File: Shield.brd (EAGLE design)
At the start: 99.1 x 71.1 mm, 77 parts

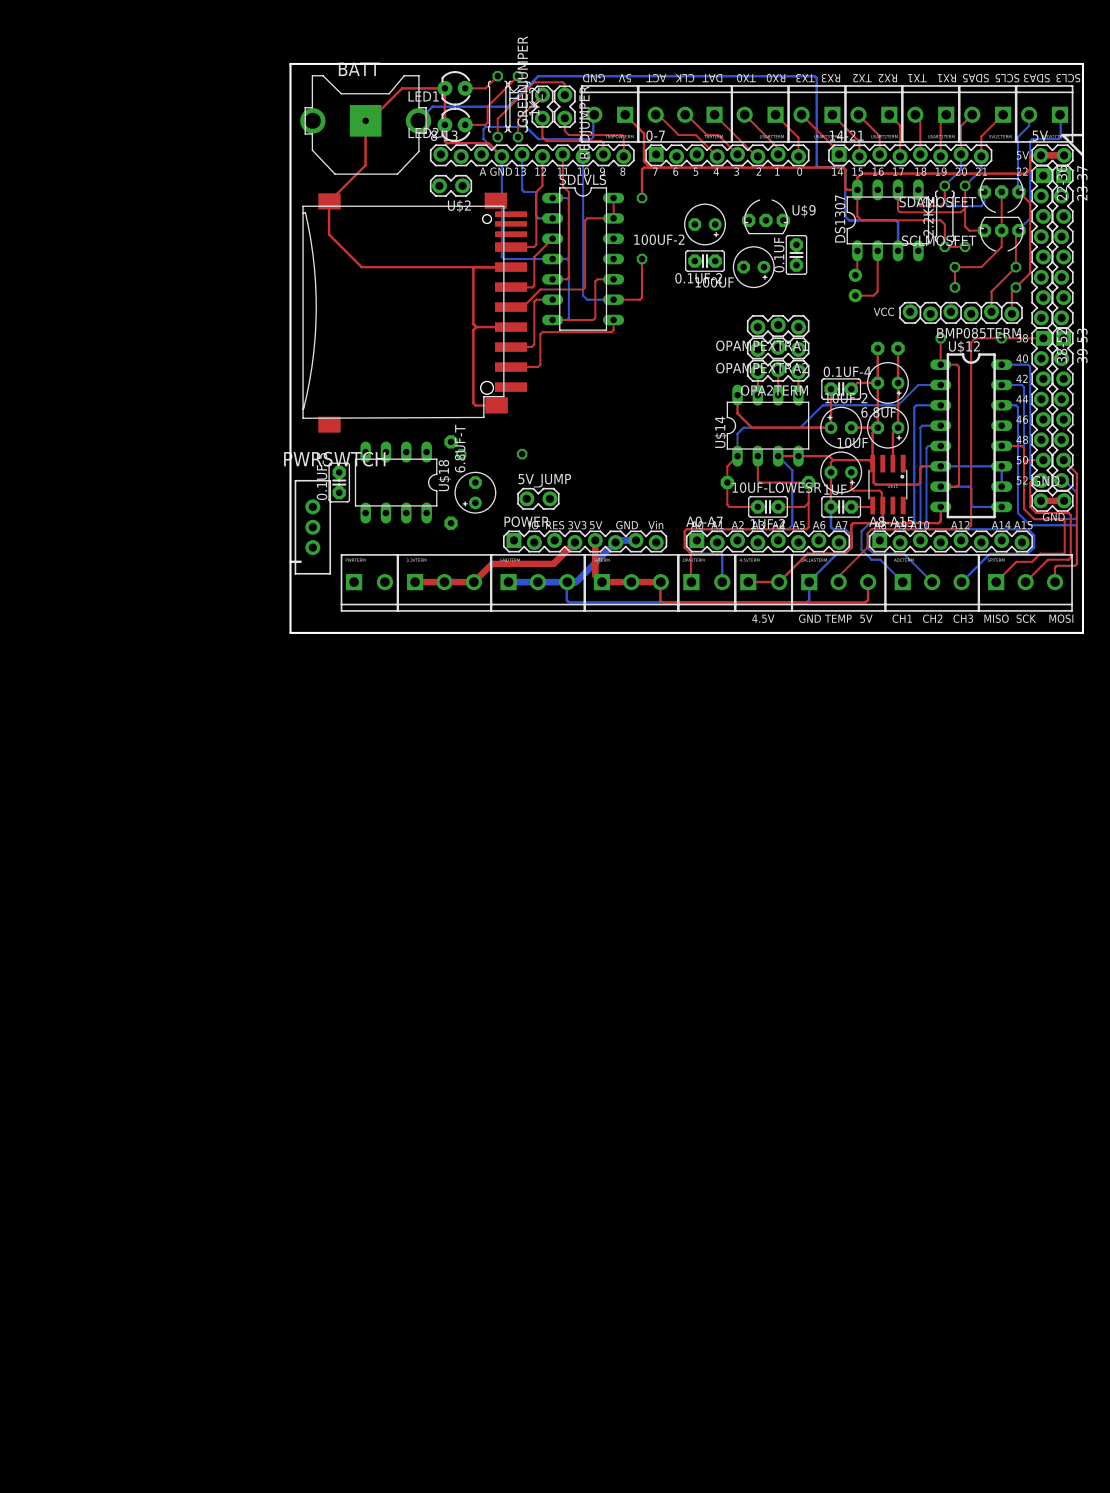
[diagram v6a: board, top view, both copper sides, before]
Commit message: Added charging circuit to schematic
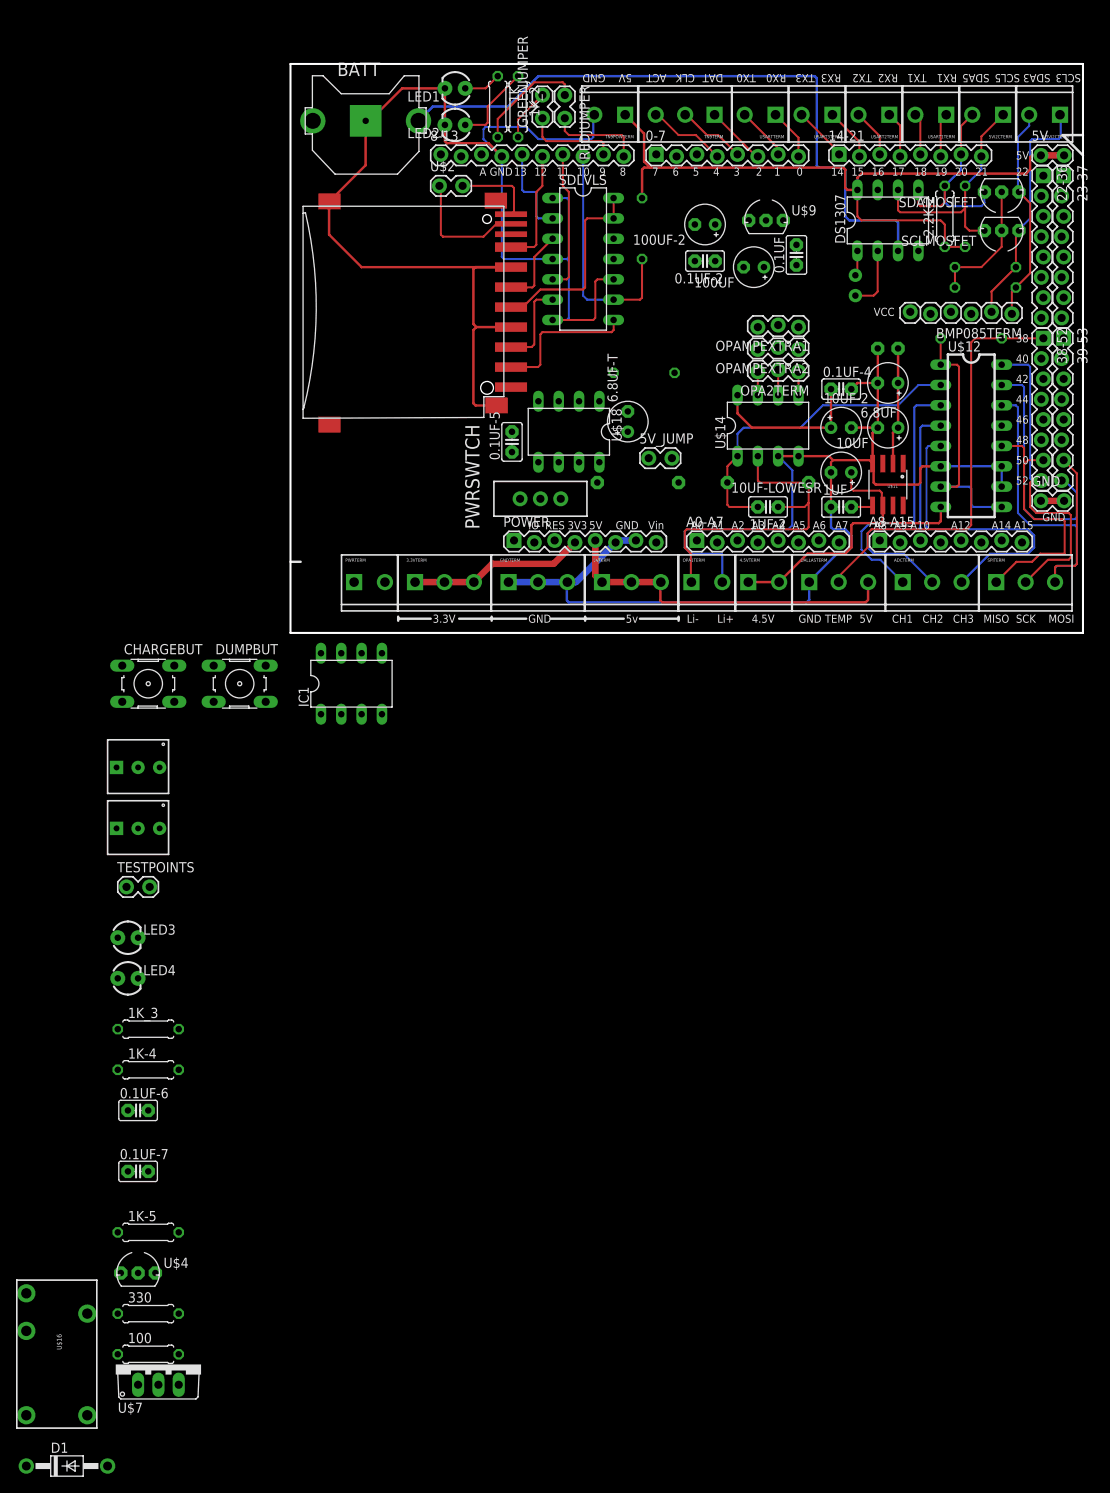
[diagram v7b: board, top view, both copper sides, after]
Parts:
- added 0.1UF-6, 0.1UF-7: CCL, LEMS:C025-025X050
- added 100, 1K-4, 1K-5, 1K_3, 330: RT, LEMS:0207/7
- added CHARGEBUT, DUMPBUT: (no value), LEMS:B3F-10XX
- added D1: 1N4004, LEMS:DO41-10
- added IC1: NE555P, LEMS:DIL-08
- added LED3, LED4: (no value), LEMS:LED3MM
- added TESTPOINTS: 2PHN, LEMS:2PH
- added TRESPOT, TRIGPOT: TRIMPOTT, LEMS:TRIMPOT_PTH_S3_LOCK
- added U$16: RELAYPTH4, LEMS:RELAY-JZC
- added U$4: 2N2222T, LEMS:TO-92INLINE
- added U$7: IRLZ34T, LEMS:TO220V
- moved PWRSWTCH 28.7 mm to (31.2, 16.8), turned to 90 degrees
- moved 250K 23.4 mm to (43.4, 18.8), turned to 180 degrees
- moved U$18 22.5 mm to (34.8, 25.1)
- moved 0.1UF-5 22.2 mm to (27.7, 23.9)
- moved 1 21.6 mm to (44.2, 32.5)
- moved 6.8UF-T 21.0 mm to (42.2, 26.4)
- moved 5V_JUMP 16.1 mm to (46.2, 21.8)
- turned U$2 to 0 degrees
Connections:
- new net 555OUT: 1K-4.2, 1K-5.1, IC1.3
- new net DIS: IC1.7, LED3.K
- new net DUMMY: U$16.2
- new net N$10: 1K-4.1, LED4.A
- new net N$11: 100.1, 330.1, U$4.1
- new net N$12: 1K-5.2, U$4.2
- new net N$13: 100.2, U$7.1
- new net N$15: D1.A, U$16.1, U$7.2
- new net N$8: 1K_3.1, LED3.A
- new net N$9: 0.1UF-7.1, IC1.5
- new net SLRIN: U$16.4
- new net TP1: CHARGEBUT.3, CHARGEBUT.4, IC1.2, TESTPOINTS.1, TRIGPOT.2
- new net TP2: DUMPBUT.3, DUMPBUT.4, IC1.6, TESTPOINTS.2, TRESPOT.2
- net 5V: now also 0.1UF-6.2, 1K_3.2, 330.2, DUMPBUT.1, DUMPBUT.2, IC1.4, IC1.8
- net GND: now also 0.1UF-6.1, 0.1UF-7.2, CHARGEBUT.1, CHARGEBUT.2, IC1.1, LED4.K, TRESPOT.3, TRIGPOT.3, U$4.3, U$7.3
- net PWRN: now also D1.C, TRESPOT.1, TRIGPOT.1, U$16.3, U$16.5
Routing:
- net SD_CD: track 0.00 -> 15.7 mm
- net SD_WP: track 0.00 -> 9.98 mm
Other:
- board text added: "3.3V"
- board text added: "5v"
- board text added: "Li+"
- board text added: "Li-"

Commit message: Changed charging circuit, finished routing
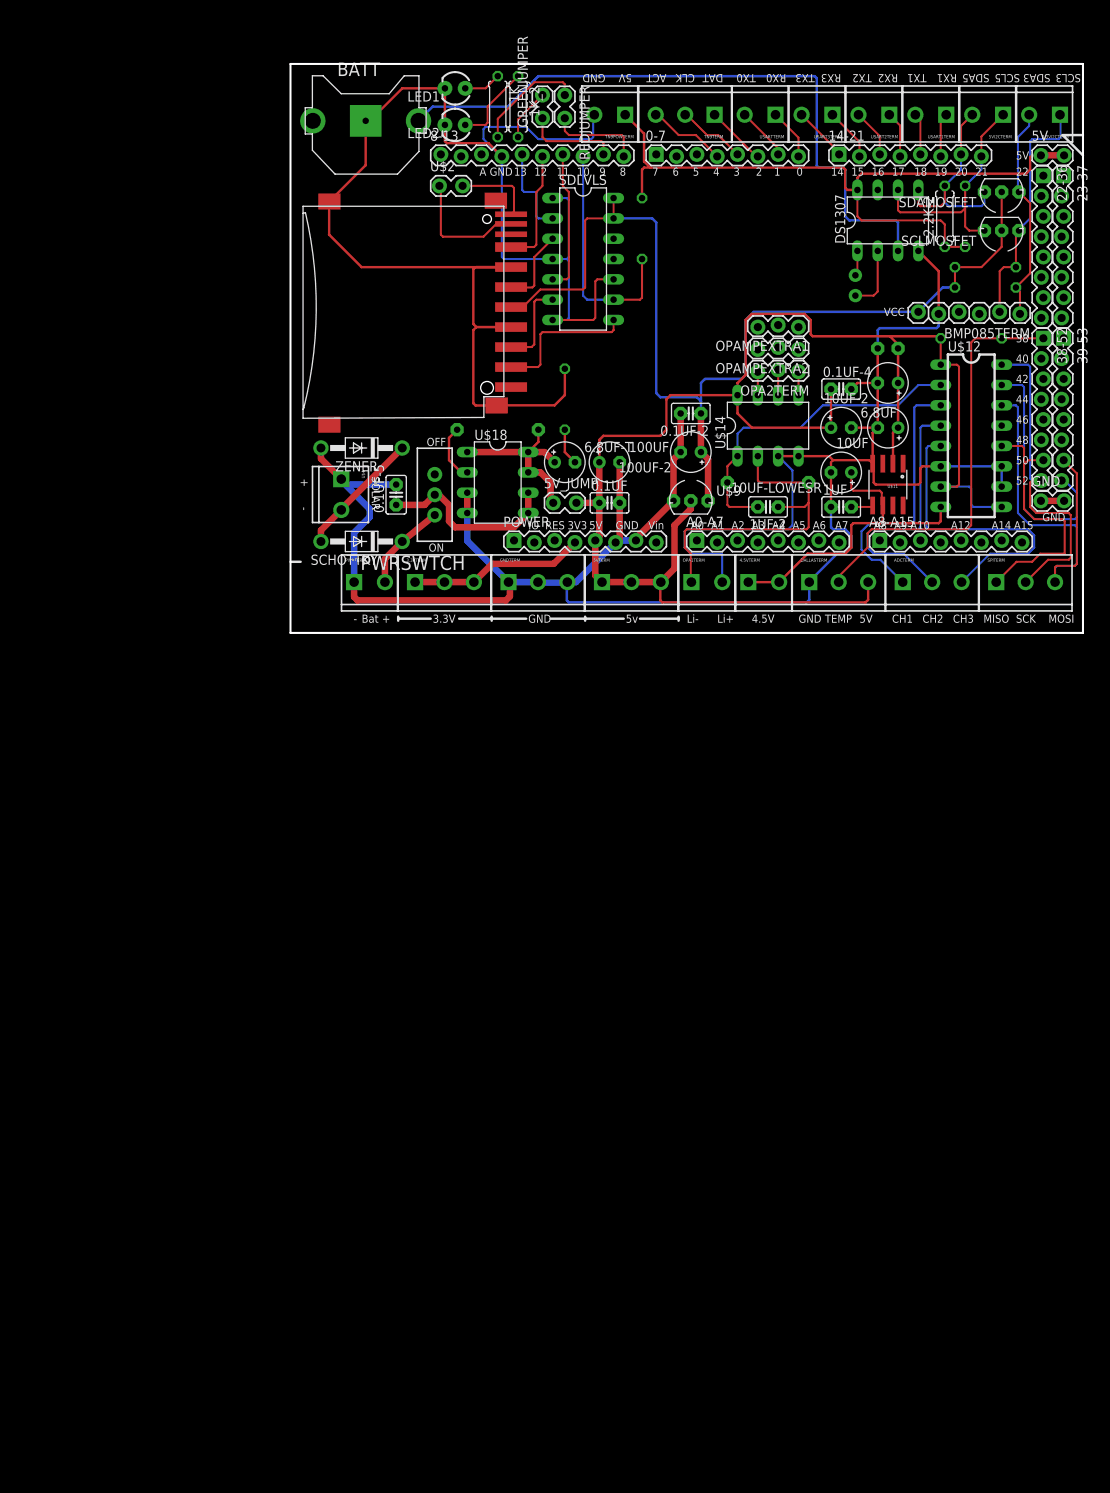
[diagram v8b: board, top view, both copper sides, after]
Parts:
- removed 0.1UF-6, 0.1UF-7: CCL, LEMS:C025-025X050
- removed 100, 1K-4, 1K-5, 1K_3, 330: RT, LEMS:0207/7
- removed CHARGEBUT, DUMPBUT: (no value), LEMS:B3F-10XX
- removed D1: 1N4004, LEMS:DO41-10
- removed IC1: NE555P, LEMS:DIL-08
- removed LED3, LED4: (no value), LEMS:LED3MM
- removed TESTPOINTS: 2PHN, LEMS:2PH
- removed TRESPOT, TRIGPOT: TRIMPOTT, LEMS:TRIMPOT_PTH_S3_LOCK
- removed U$16: RELAYPTH4, LEMS:RELAY-JZC
- removed U$7: IRLZ34T, LEMS:TO220V
- added SCHOTTKY: (no value), adafruit:DO41-10
- added ZENER: 1N4004, LEMS:DO41-10
- U$4: value 2N2222T -> 2PHS; device LEMS:TO-92INLINE -> LEMS:SCREWTERMINAL-3.5MM-2_LOCK
- moved U$4 102.3 mm to (6.35, 19.1), turned to 270 degrees
- moved 0.1UF 38.8 mm to (39.9, 16.3), turned to 0 degrees
- moved U$9 36.3 mm to (50.0, 16.5)
- moved 100UF 30.3 mm to (39.9, 21.3), turned to 0 degrees
- moved 100UF-2 28.5 mm to (50.0, 22.6)
- moved 0.1UF-2 19.1 mm to (50.0, 27.4)
- moved 250K 18.7 mm to (25.9, 25.4)
- moved 0.1UF-5 15.9 mm to (13.2, 17.3)
- moved PWRSWTCH 13.2 mm to (18.0, 17.3), turned to 180 degrees
- moved 5V_JUMP 13.2 mm to (34.3, 16.3)
- moved U$18 10.9 mm to (25.9, 18.8), turned to 270 degrees
- moved 1 10.4 mm to (34.3, 29.2), turned to 270 degrees
- moved 6.8UF-T 9.37 mm to (34.3, 21.3), turned to 0 degrees
- moved BMP085TERM 1.02 mm to (84.8, 39.9)
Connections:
- removed net 555OUT: 1K-4.2, 1K-5.1, IC1.3
- removed net DIS: IC1.7, LED3.K
- removed net DUMMY: U$16.2
- removed net N$10: 1K-4.1, LED4.A
- removed net N$11: 100.1, 330.1, U$4.1
- removed net N$12: 1K-5.2, U$4.2
- removed net N$13: 100.2, U$7.1
- removed net N$15: D1.A, U$16.1, U$7.2
- removed net N$8: 1K_3.1, LED3.A
- removed net N$9: 0.1UF-7.1, IC1.5
- removed net SLRIN: U$16.4
- removed net TP1: CHARGEBUT.3, CHARGEBUT.4, IC1.2, TESTPOINTS.1, TRIGPOT.2
- removed net TP2: DUMPBUT.3, DUMPBUT.4, IC1.6, TESTPOINTS.2, TRESPOT.2
- new net SOLRPOS: SCHOTTKY.A, U$4.2, ZENER.C
- net 5V: no longer 0.1UF-6.2, 1K_3.2, 330.2, DUMPBUT.1, DUMPBUT.2, IC1.4, IC1.8
- net GND: now also U$4.1, ZENER.A; no longer 0.1UF-6.1, 0.1UF-7.2, CHARGEBUT.1, CHARGEBUT.2, IC1.1, LED4.K, TRESPOT.3, TRIGPOT.3, U$4.3, U$7.3
- net PWRN: now also SCHOTTKY.C; no longer D1.C, TRESPOT.1, TRIGPOT.1, U$16.3, U$16.5
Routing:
- net GND: track 334.9 -> 460.9 mm
- net 3.3V: track 41.1 -> 129.9 mm
- net 5V: track 200.9 -> 288.8 mm
- net 5VOUT: track 0.00 -> 23.3 mm
- net REG_IN: track 0.00 -> 23.2 mm
- net SOLRPOS: track 0.00 -> 15.9 mm
- net PWRN: track 0.00 -> 11.2 mm
- net N$6: track 0.00 -> 7.15 mm
- net N$7: track 0.00 -> 4.59 mm
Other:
- board text added: "+"
- board text added: "-"
- board text added: "Bat"
- board text added: "OFF"
- board text added: "ON"
- board text added: "SOLAR"
